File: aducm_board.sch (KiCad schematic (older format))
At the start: 32 parts, among them J1 Conn_02x04_Odd_Even, SW1 SW_Push, U1 aducm_355, Y1 32MHz

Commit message: ready for check by another person
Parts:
- added J4: USB_C_Receptacle_USB2.0, Connector_USB:USB_C_Receptacle_Amphenol_12401610E4-2A, symbol Connector:USB_C_Receptacle_USB2.0
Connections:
- net FTDI/5VUSB: now also J4.A4 (VBUS), J4.A9 (VBUS), J4.B4 (VBUS), J4.B9 (VBUS)
- net FTDI/USBD+: now also J4.A6 (D+), J4.B6 (D+)
- net FTDI/USBD-: now also J4.A7 (D-), J4.B7 (D-)
- net GNDA: now also J4.A1 (GND), J4.A12 (GND), J4.B1 (GND), J4.B12 (GND)
- net P0.0_SCLK0: no longer names the net of U1.H9 (P0.0/SPI0_CLK)
- net P0.1_SPI0_MOSI: no longer names the net of U1.H8 (P0.1/SPI_MOSI)
- net P0.2_SPI0_MISO: no longer names the net of U1.H7 (P0.2/SPI0_MISO)
- net P1.5_CS: no longer names the net of U1.D6 (P1.5/SPI1_~CS)
- no-connect marks 1 -> 6
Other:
- note added: "Amphenol 12401598E4#2A"
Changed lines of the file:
@@
 Wire Wire Line
 	8700 3700 8850 3700
-Text Label 8700 4300 2    50   ~ 0
-P1.5_CS
-Wire Wire Line
-	8700 4300 8850 4300
 Text Label 11400 5450 0    50   ~ 0
 CAP_POT0
@@
 Wire Wire Line
 	8850 6100 8550 6100
-Text Label 8700 3000 2    50   ~ 0
-P0.0_SCLK0
-Wire Wire Line
-	8850 3000 8700 3000
-Text Label 8700 3100 2    50   ~ 0
-P0.1_SPI0_MOSI
-Wire Wire Line
-	8850 3100 8700 3100
-Text Label 8700 3200 2    50   ~ 0
-P0.2_SPI0_MISO
-Wire Wire Line
-	8700 3200 8850 3200
 Text Label 11400 2800 0    50   ~ 0
 ~RESET
@@
 	1600 1150 1700 1150
 $Sheet
-S 2600 6150 950  950
+S 3050 5650 950  950
 U 5EBF9349
 F0 "FTDI" 50
 F1 "FTDI.sch" 50
-F2 "USBD+" I L 2600 6350 50
-F3 "USBD-" I L 2600 6550 50
-F4 "SIN" I R 3550 6350 50
-F5 "SOUT" I R 3550 6600 50
-F6 "5VUSB" I L 2600 6850 50
-F7 "DGND" I L 2600 6950 50
+F2 "USBD+" I L 3050 6200 50
+F3 "USBD-" I L 3050 6000 50
+F4 "SIN" I R 4000 5950 50
+F5 "SOUT" I R 4000 6100 50
+F6 "5VUSB" I L 3050 5800 50
+F7 "DGND" I L 3050 6350 50
+F8 "3V3VDD" B R 4000 5800 50
 $EndSheet
 $Comp
@@
 	1    0    0    -1
 $EndComp
+$Comp
+L Connector:USB_C_Receptacle_USB2.0 J4
+U 1 1 5EC8B4AC
+P 2000 6100
+F 0 "J4" H 2107 6967 50  0000 C CNN
+F 1 "USB_C_Receptacle_USB2.0" H 2107 6876 50  0000 C CNN
+F 2 "Connector_USB:USB_C_Receptacle_Amphenol_12401610E4-2A" H 2150 6100 50  0001 C CNN
+F 3 "https://www.usb.org/sites/default/files/documents/usb_type-c.zip" H 2150 6100 50  0001 C CNN
+	1    2000 6100
+	1    0    0    -1
+$EndComp
+Wire Wire Line
+	2600 5500 2950 5500
+Wire Wire Line
+	2950 5500 2950 5800
+Wire Wire Line
+	2950 5800 3050 5800
+Wire Wire Line
+	2600 6000 2600 6050
+Wire Wire Line
+	2600 6200 2600 6250
+Wire Wire Line
+	3050 6000 2850 6000
+Wire Wire Line
+	2850 6000 2850 6050
+Wire Wire Line
+	2850 6050 2600 6050
+Connection ~ 2600 6050
+Wire Wire Line
+	2600 6050 2600 6100
+Wire Wire Line
+	3050 6200 2850 6200
+Wire Wire Line
+	2850 6200 2850 6250
+Wire Wire Line
+	2850 6250 2600 6250
+Connection ~ 2600 6250
+Wire Wire Line
+	2600 6250 2600 6300
+Wire Wire Line
+	3050 6350 2900 6350
+Wire Wire Line
+	2900 6350 2900 7000
+Wire Wire Line
+	2900 7000 2450 7000
+Text GLabel 2450 7150 3    50   Input ~ 0
+DGND
+Wire Wire Line
+	2450 7150 2450 7000
+Connection ~ 2450 7000
+Wire Wire Line
+	2450 7000 2000 7000
+Text Label 4350 6100 0    50   ~ 0
+UART_SOUT
+Wire Wire Line
+	4350 6100 4000 6100
+Text Label 4350 5950 0    50   ~ 0
+UART_SIN
+Wire Wire Line
+	4350 5950 4000 5950
+Text GLabel 4350 5800 2    50   Input ~ 0
+DVDD
+Wire Wire Line
+	4350 5800 4000 5800
+NoConn ~ 1700 7000
+NoConn ~ 2600 5800
+NoConn ~ 2600 5700
+NoConn ~ 2600 6700
+NoConn ~ 2600 6600
+Text Notes 1700 5200 0    50   ~ 0
+Amphenol 12401598E4#2A
 $EndSCHEMATC

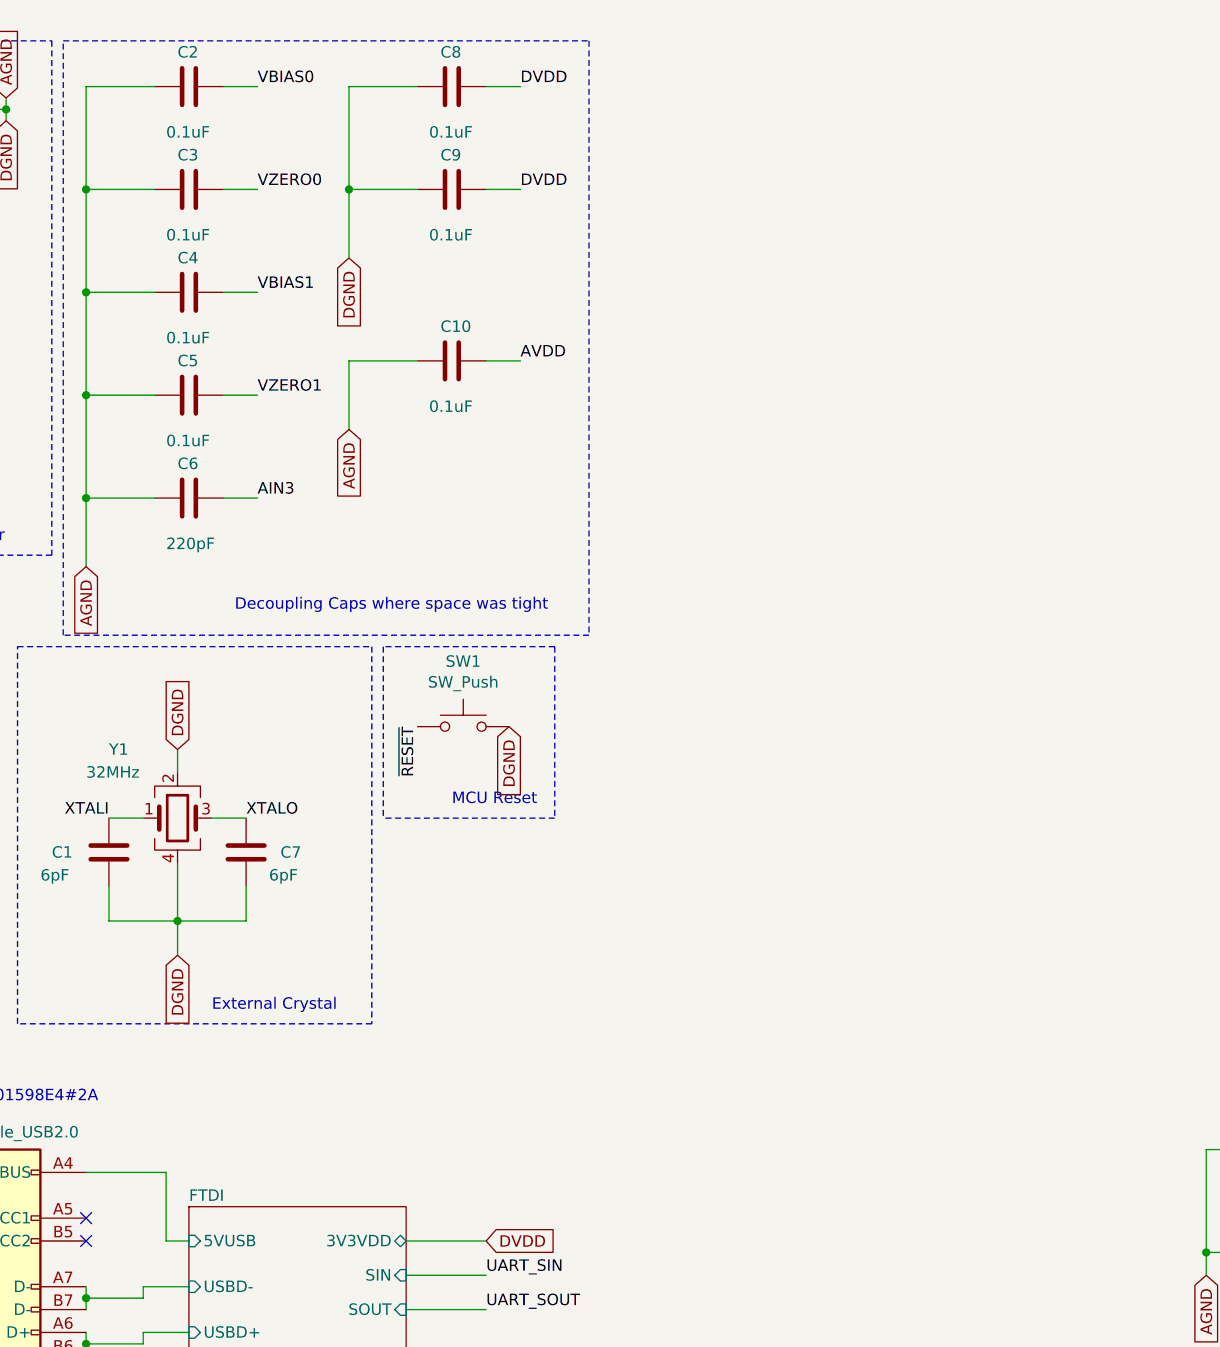
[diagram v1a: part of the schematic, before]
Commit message: usb power added
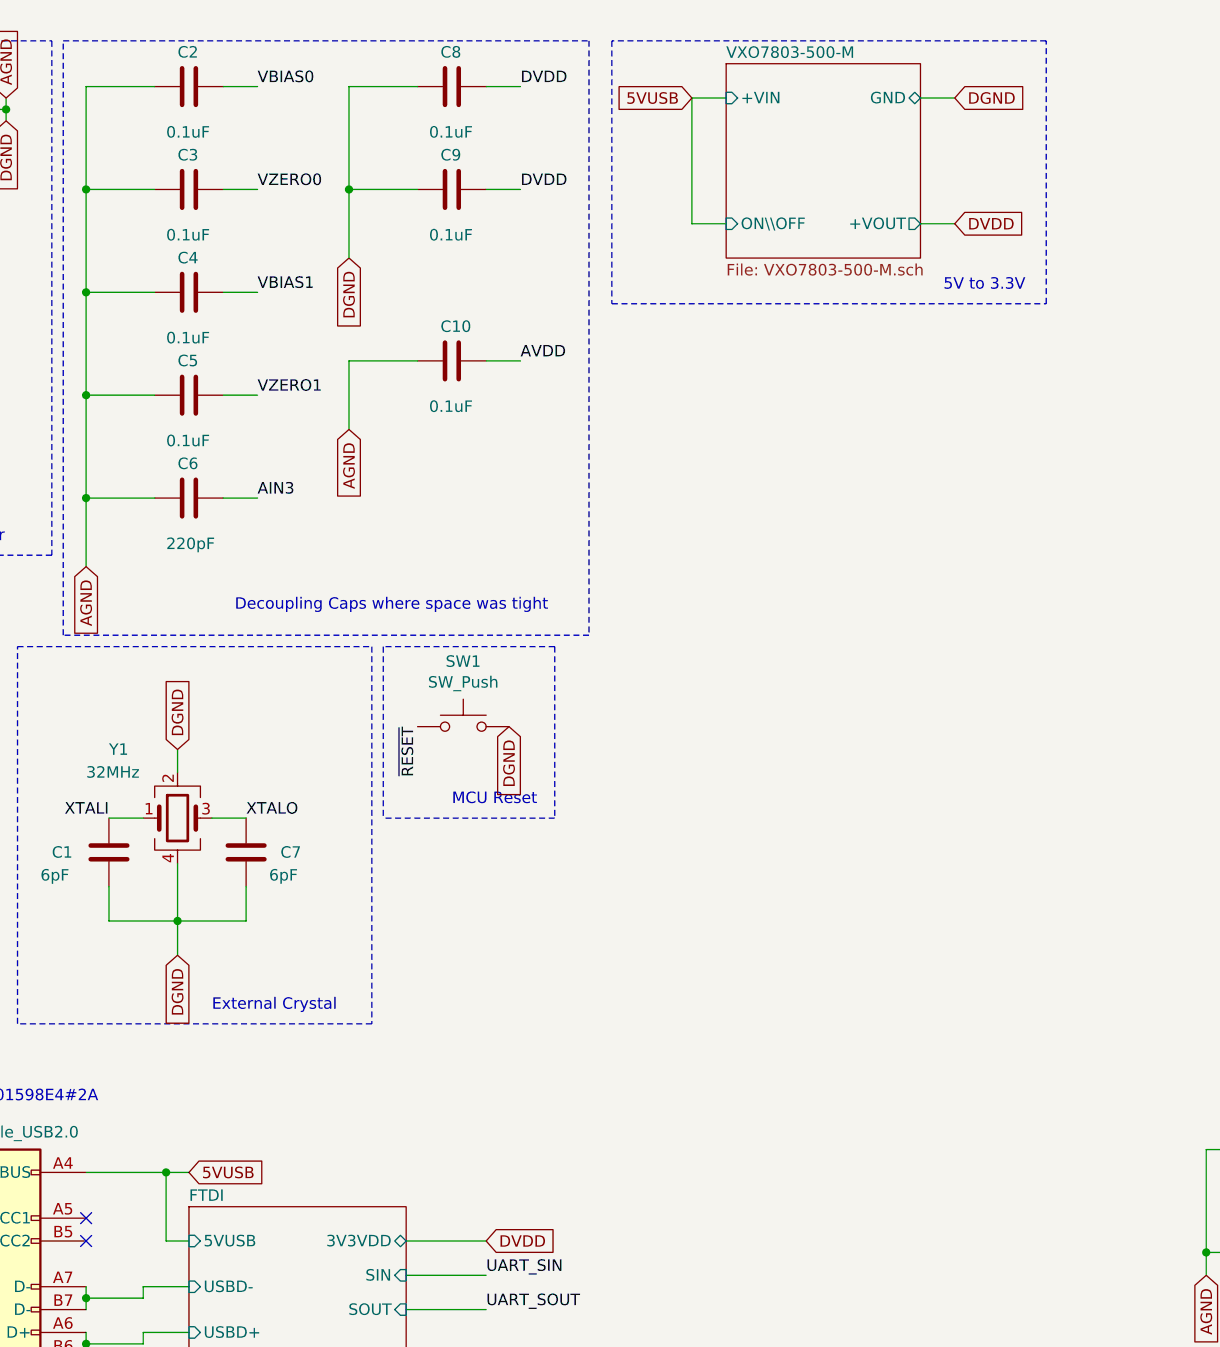
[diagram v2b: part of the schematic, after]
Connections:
- net FTDI/5VUSB renamed 5VUSB
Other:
- note added: "5V to 3.3V"
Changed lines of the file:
@@
 EESchema Schematic File Version 4
-EELAYER 30 0
+EELAYER 26 0
 EELAYER END
 $Descr A3 16535 11693
 encoding utf-8
-Sheet 1 4
+Sheet 1 5
 Title "ADuCM355 Template"
 Date ""
@@
 Text Notes 1700 5200 0    50   ~ 0
 Amphenol 12401598E4#2A
+$Sheet
+S 5400 650  850  850
+U 5ED209B3
+F0 "VXO7803-500-M" 50
+F1 "VXO7803-500-M.sch" 50
+F2 "+VIN" I L 5400 800 50
+F3 "+VOUT" O R 6250 1350 50
+F4 "ON\\OFF" I L 5400 1350 50
+F5 "GND" B R 6250 800 50
+$EndSheet
+Text GLabel 3050 5500 2    50   Input ~ 0
+5VUSB
+Wire Wire Line
+	3050 5500 2950 5500
+Connection ~ 2950 5500
+Text GLabel 5250 800  0    50   Input ~ 0
+5VUSB
+Wire Wire Line
+	5400 800  5250 800
+Text GLabel 6400 800  2    50   Input ~ 0
+DGND
+Wire Wire Line
+	6400 800  6250 800
+Wire Wire Line
+	6400 1350 6250 1350
+Text GLabel 6400 1350 2    50   Input ~ 0
+DVDD
+Wire Wire Line
+	5250 800  5250 1350
+Wire Wire Line
+	5250 1350 5400 1350
+Wire Notes Line
+	6800 1700 6800 550
+Wire Notes Line
+	6800 550  4900 550
+Wire Notes Line
+	4900 550  4900 1700
+Wire Notes Line
+	4900 1700 6800 1700
+Text Notes 6350 1650 0    50   ~ 0
+5V to 3.3V
 $EndSCHEMATC

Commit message: updating sib-kicad-footprint commit
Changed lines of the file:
@@
 EESchema Schematic File Version 4
 LIBS:aducm_board-cache
-EELAYER 26 0
+EELAYER 30 0
 EELAYER END
 $Descr A3 16535 11693
@@
 F6 "5VUSB" I L 3050 5800 50
 F7 "DGND" I L 3050 6350 50
-F8 "3V3VDD" B R 4000 5800 50
 $EndSheet
 $Comp
@@
 Wire Wire Line
 	4350 5950 4000 5950
-Text GLabel 4350 5800 2    50   Input ~ 0
-DVDD
-Wire Wire Line
-	4350 5800 4000 5800
 NoConn ~ 1700 7000
 NoConn ~ 2600 5800

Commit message: switched 6 pin jtag to 20 pin jtag
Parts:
- J1: footprint Connector_PinHeader_2.54mm:PinHeader_2x04_P2.54mm_Horizontal -> Connector_PinHeader_2.54mm:PinHeader_2x10_P2.54mm_Vertical; symbol Connector_Generic:Conn_02x04_Odd_Even -> Connector_Generic:Conn_02x10_Odd_Even
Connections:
- wire segments 169 -> 180
- no-connect marks 6 -> 9
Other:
- note added: "20-pin J-Tag Connector"
- note removed: "6-pin J-Tag Connector"
- moved on the sheet: R1, R2
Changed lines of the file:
@@
 	2300 4850 2300 3200
 $Comp
-L Connector_Generic:Conn_02x04_Odd_Even J1
+L Connector_Generic:Conn_02x10_Odd_Even J1
 U 1 1 5E1C696B
-P 1250 950
-F 0 "J1" H 1300 1267 50  0000 C CNN
-F 1 "Conn_02x04_Odd_Even" H 1300 1176 50  0000 C CNN
-F 2 "Connector_PinHeader_2.54mm:PinHeader_2x04_P2.54mm_Horizontal" H 1250 950 50  0001 C CNN
-F 3 "~" H 1250 950 50  0001 C CNN
-	1    1250 950
-	1    0    0    -1
-$EndComp
-Text Label 900  850  2    50   ~ 0
+P 1750 1550
+F 0 "J1" H 1800 1867 50  0000 C CNN
+F 1 "Conn_02x04_Odd_Even" V 1300 900 50  0001 C CNN
+F 2 "Connector_PinHeader_2.54mm:PinHeader_2x10_P2.54mm_Vertical" H 1750 1550 50  0001 C CNN
+F 3 "~" H 1750 1550 50  0001 C CNN
+	1    1750 1550
+	1    0    0    -1
+$EndComp
+Text Label 1450 1850 2    50   ~ 0
 ~RESET
-Wire Wire Line
-	900  850  1050 850
-Text Label 900  950  2    50   ~ 0
+Text Label 1450 1450 2    50   ~ 0
 SWDIO
-Text Label 900  1050 2    50   ~ 0
+Text Label 1450 1550 2    50   ~ 0
 SWCLK
-Text Label 1700 950  0    50   ~ 0
+Text Label 1450 1950 2    50   ~ 0
 UART_SOUT
-Text Label 1700 1050 0    50   ~ 0
+Text Label 1450 1350 2    50   ~ 0
 UART_SIN
-Text GLabel 2250 900  3    50   Input ~ 0
+Text GLabel 2350 1500 3    50   Input ~ 0
 DGND
 Wire Wire Line
-	1550 950  1700 950
-Wire Wire Line
-	1700 1050 1550 1050
-Wire Wire Line
-	1550 1150 1600 1150
-Wire Wire Line
-	1050 1050 900  1050
-Wire Wire Line
-	900  950  1050 950
+	1550 1950 1450 1950
+Wire Wire Line
+	1450 1350 1550 1350
 Wire Notes Line
 	550  550  2450 550
 Text Notes 1500 2750 0    50   ~ 0
-6-pin J-Tag Connector
+20-pin J-Tag Connector
 $Comp
 L Device:R_Small_US R1
 U 1 1 5E26FED1
-P 1250 2100
-F 0 "R1" H 1050 2150 50  0000 L CNN
-F 1 "100k" H 1000 2050 50  0000 L CNN
-F 2 "Resistor_SMD:R_0603_1608Metric" H 1250 2100 50  0001 C CNN
-F 3 "~" H 1250 2100 50  0001 C CNN
-	1    1250 2100
+P 800 2300
+F 0 "R1" H 600 2350 50  0000 L CNN
+F 1 "100k" H 550 2250 50  0000 L CNN
+F 2 "Resistor_SMD:R_0603_1608Metric" H 800 2300 50  0001 C CNN
+F 3 "~" H 800 2300 50  0001 C CNN
+	1    800  2300
 	1    0    0    -1
 $EndComp
@@
 L Device:R_Small_US R2
 U 1 1 5E29740B
-P 1600 2100
-F 0 "R2" H 1400 2150 50  0000 L CNN
-F 1 "100k" H 1350 2050 50  0000 L CNN
-F 2 "Resistor_SMD:R_0603_1608Metric" H 1600 2100 50  0001 C CNN
-F 3 "~" H 1600 2100 50  0001 C CNN
-	1    1600 2100
-	1    0    0    -1
-$EndComp
-Text GLabel 1700 1150 2    50   Input ~ 0
+P 1150 2300
+F 0 "R2" H 950 2350 50  0000 L CNN
+F 1 "100k" H 900 2250 50  0000 L CNN
+F 2 "Resistor_SMD:R_0603_1608Metric" H 1150 2300 50  0001 C CNN
+F 3 "~" H 1150 2300 50  0001 C CNN
+	1    1150 2300
+	1    0    0    -1
+$EndComp
+Text GLabel 1750 1000 1    50   Input ~ 0
 DVDD
-Text GLabel 1450 1750 1    50   Input ~ 0
+Text GLabel 1000 1850 1    50   Input ~ 0
 DVDD
 Wire Wire Line
-	1250 2000 1250 1900
-Text Label 1250 2350 3    50   ~ 0
+	800  2200 800  2100
+Text Label 800  2550 3    50   ~ 0
 SWDIO
 Wire Wire Line
-	1250 2350 1250 2200
-Text Label 1600 2350 3    50   ~ 0
+	800  2550 800  2400
+Text Label 1150 2550 3    50   ~ 0
 SWCLK
 Wire Wire Line
-	1600 2200 1600 2350
-Wire Wire Line
-	1250 1900 1450 1900
-Wire Wire Line
-	1450 1900 1450 1750
-Wire Wire Line
-	1450 1900 1600 1900
-Connection ~ 1450 1900
-Wire Wire Line
-	1600 1900 1600 2000
+	1150 2400 1150 2550
+Wire Wire Line
+	800  2100 1000 2100
+Wire Wire Line
+	1000 2100 1000 1850
+Wire Wire Line
+	1000 2100 1150 2100
+Connection ~ 1000 2100
+Wire Wire Line
+	1150 2100 1150 2200
 Wire Notes Line
 	2450 2800 550  2800
@@
 Wire Notes Line
 	550  550  550  2800
-Wire Wire Line
-	1550 850  2250 850
-Wire Wire Line
-	2250 850  2250 900
 Wire Notes Line
 	1550 2850 550  2850
@@
 Wire Wire Line
 	11250 5900 12300 5900
-NoConn ~ 1050 1150
 Text Label 12100 6100 0    50   ~ 0
 VBIAS1
@@
 Text GLabel 1300 3200 0    50   Input ~ 0
 AGND
-Wire Wire Line
-	2250 800  2250 850
-Connection ~ 2250 850
 Text Label 8400 5300 0    50   ~ 0
 AIN3
 Wire Wire Line
 	8400 5300 8850 5300
-Text GLabel 2250 800  1    50   Input ~ 0
+Text GLabel 2350 1400 1    50   Input ~ 0
 AGND
-Text GLabel 1700 1250 2    50   Input ~ 0
+Text GLabel 1850 1000 1    50   Input ~ 0
 AVDD
-Wire Wire Line
-	1700 1250 1600 1250
-Wire Wire Line
-	1600 1250 1600 1150
-Connection ~ 1600 1150
-Wire Wire Line
-	1600 1150 1700 1150
 $Sheet
 S 3050 5650 950  950
@@
 Text Notes 6350 1650 0    50   ~ 0
 5V to 3.3V
+Wire Wire Line
+	1450 1850 1550 1850
+Wire Wire Line
+	1450 1450 1550 1450
+Wire Wire Line
+	1450 1550 1550 1550
+Wire Wire Line
+	2350 1400 2350 1450
+Wire Wire Line
+	1750 1000 1800 1000
+Wire Wire Line
+	1800 1000 1800 1050
+Connection ~ 1800 1000
+Wire Wire Line
+	1800 1000 1850 1000
+Wire Wire Line
+	2050 2050 2050 1950
+Wire Wire Line
+	2050 1950 2050 1850
+Connection ~ 2050 1950
+Wire Wire Line
+	2050 1850 2050 1750
+Connection ~ 2050 1850
+Wire Wire Line
+	2050 1750 2050 1650
+Connection ~ 2050 1750
+Wire Wire Line
+	2050 1550 2050 1650
+Connection ~ 2050 1650
+Wire Wire Line
+	2050 1250 2050 1350
+Wire Wire Line
+	2050 1350 2050 1450
+Connection ~ 2050 1350
+Wire Wire Line
+	2050 1450 2050 1550
+Connection ~ 2050 1450
+Connection ~ 2050 1550
+Wire Wire Line
+	2350 1450 2050 1450
+Connection ~ 2350 1450
+Wire Wire Line
+	2350 1450 2350 1500
+NoConn ~ 1550 1250
+NoConn ~ 1550 1650
+NoConn ~ 1550 1750
+NoConn ~ 1550 2050
+Wire Wire Line
+	2050 1150 2050 1050
+Wire Wire Line
+	2050 1050 1800 1050
+Wire Wire Line
+	1550 1050 1550 1150
+Connection ~ 1800 1050
+Wire Wire Line
+	1800 1050 1550 1050
 $EndSCHEMATC

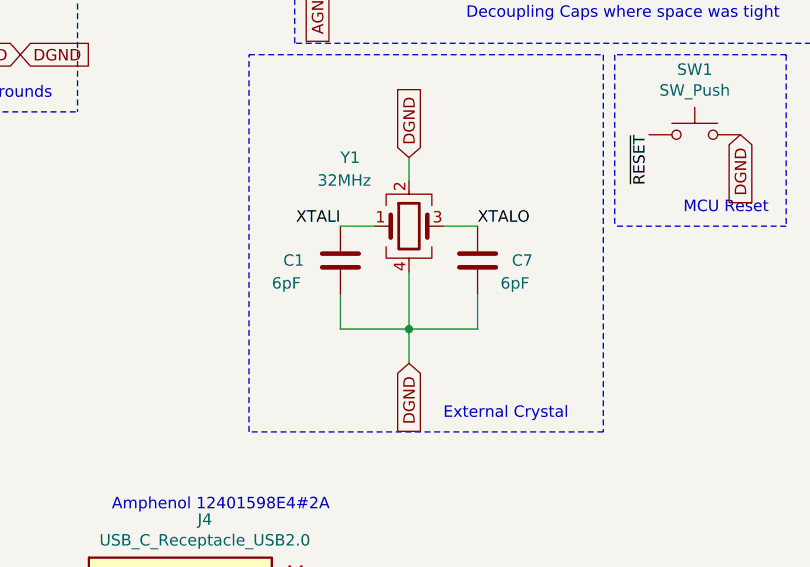
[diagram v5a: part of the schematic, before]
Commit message: fixed crystal cap and some traces
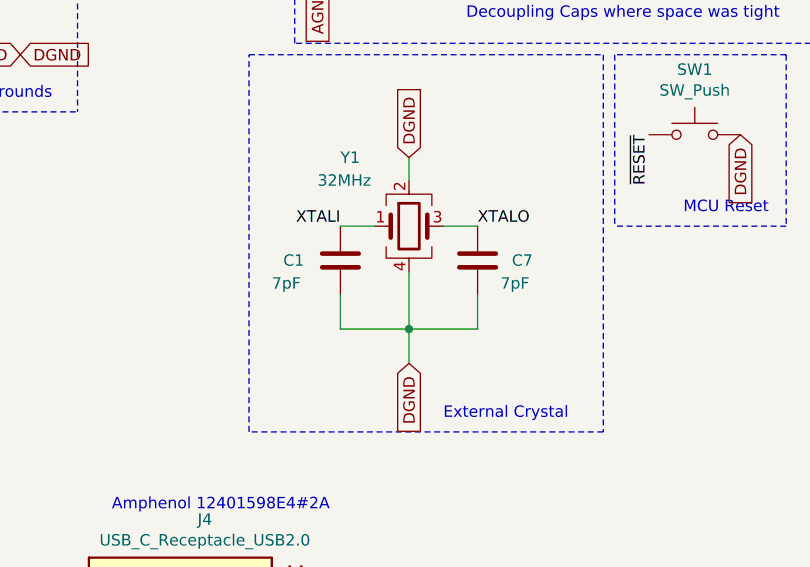
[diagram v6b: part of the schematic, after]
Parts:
- C1, C7: value 6pF -> 7pF
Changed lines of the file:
@@
 EESchema Schematic File Version 4
-LIBS:aducm_board-cache
 EELAYER 30 0
 EELAYER END
@@
 P 2700 4100
 F 0 "C1" H 2450 4100 50  0000 L CNN
-F 1 "6pF" H 2400 4000 50  0000 L CNN
+F 1 "7pF" H 2400 4000 50  0000 L CNN
 F 2 "Capacitor_SMD:C_0603_1608Metric" H 2738 3950 50  0001 C CNN
 F 3 "~" H 2700 4100 50  0001 C CNN
@@
 P 3300 4100
 F 0 "C7" H 3450 4100 50  0000 L CNN
-F 1 "6pF" H 3400 4000 50  0000 L CNN
+F 1 "7pF" H 3400 4000 50  0000 L CNN
 F 2 "Capacitor_SMD:C_0603_1608Metric" H 3338 3950 50  0001 C CNN
 F 3 "~" H 3300 4100 50  0001 C CNN

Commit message: beginning layout
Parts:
- added J5: Conn_02x25_Odd_Even, Connector_Molex:Molex_SlimStack_502430-5010_2x25_P0.40mm_Vertical, symbol Connector_Generic:Conn_02x25_Odd_Even
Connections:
- net labels added: AIN0, AIN1, AIN2, AIN5, AIN6, P0.0_SPI0_CLK, P0.1_SPI0_MOSI, P0.2_SPI0_~MISO, P0.3_SPI0_~CS, P0.4_I2C_SCL, P0.5_I2C_SDA, P1.0, P1.1, P1.2_SPI1_CLK, P1.3_SPI1_MOSI, P1.4_SPI1_MISO, P1.5_SPI1_~CS, P2.4, PWM0, PWM1
- wire segments 180 -> 250
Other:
- note added: "PIN 16 to 44 is fine.\nRest are subject to CHANGE"
